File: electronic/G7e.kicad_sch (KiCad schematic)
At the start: 17 parts

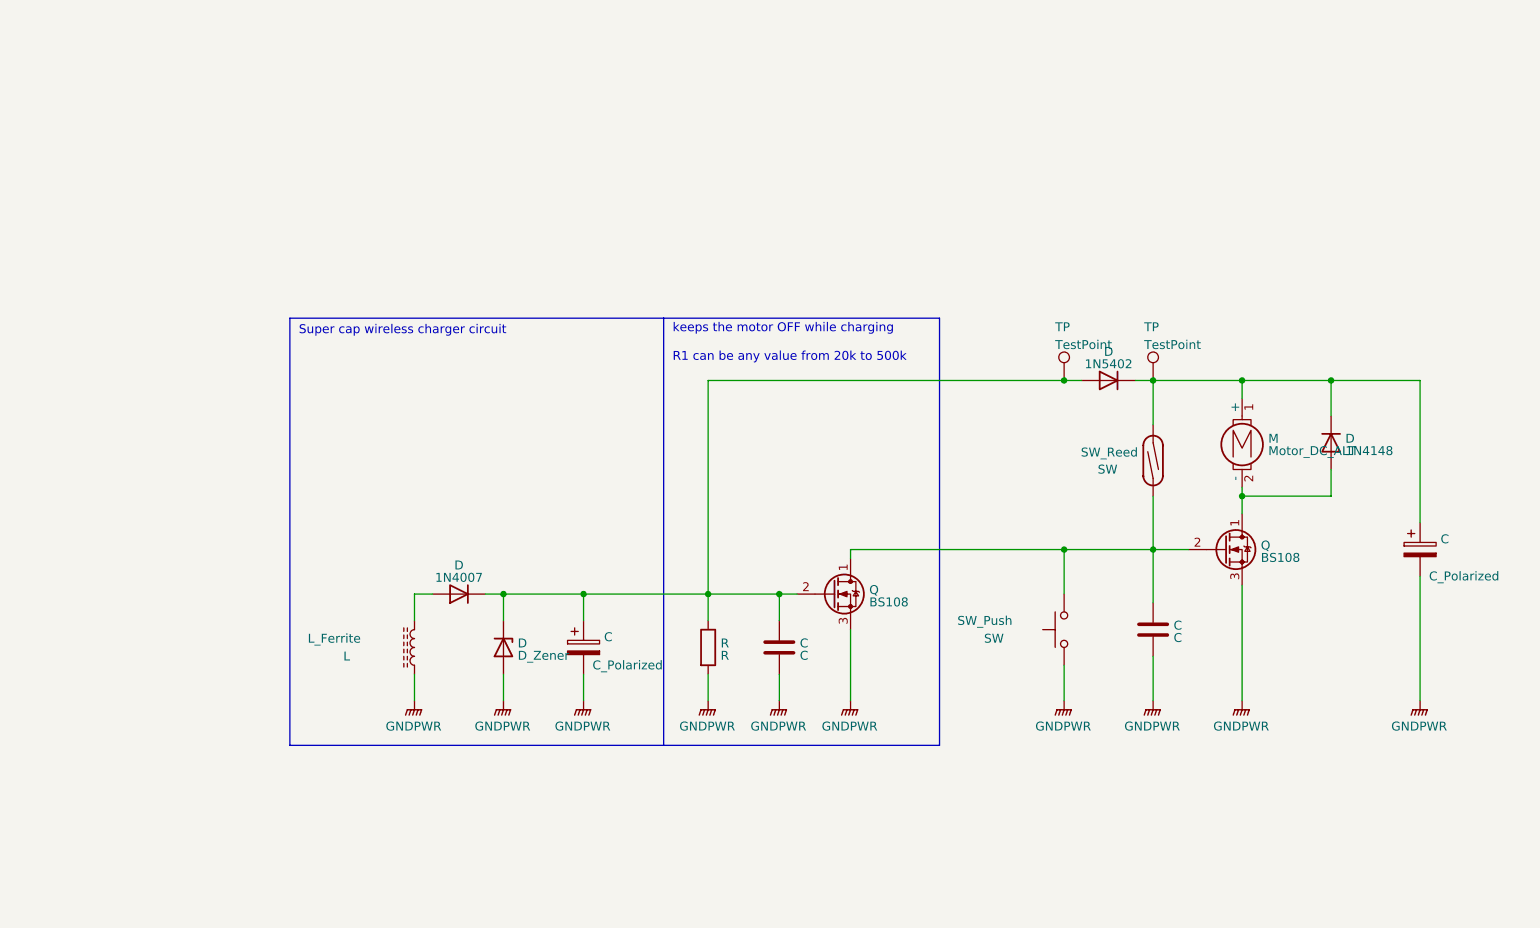
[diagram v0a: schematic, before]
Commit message: Adding propellers mockup
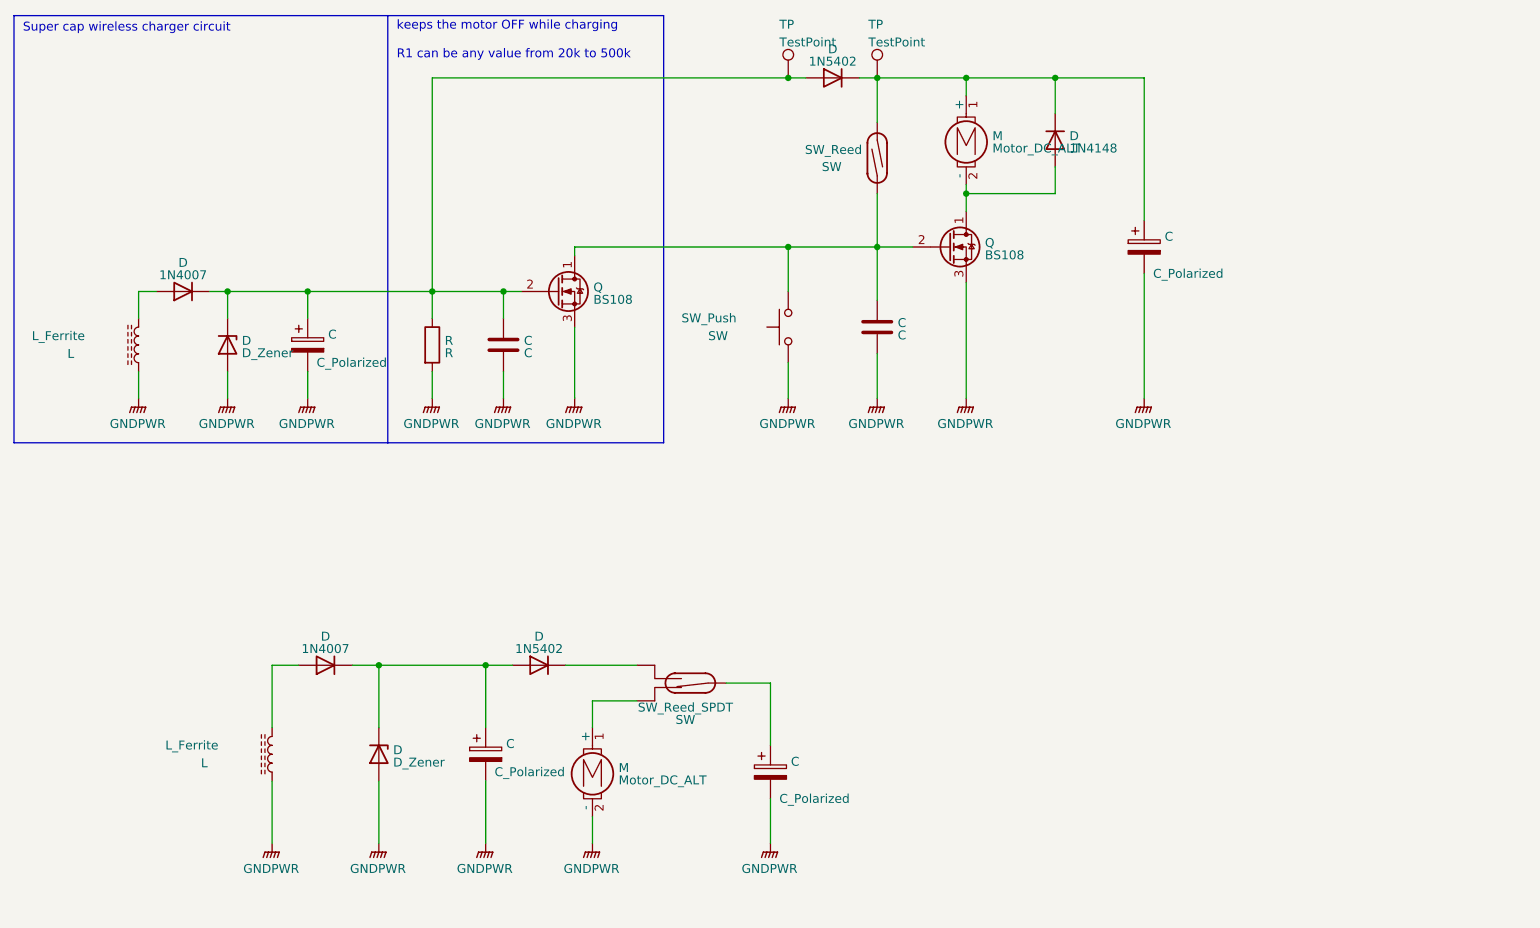
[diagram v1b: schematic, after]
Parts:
- added C (x2): C_Polarized, symbol Device:C_Polarized
- added D: 1N5402, Diode_THT:D_DO-201AD_P15.24mm_Horizontal, symbol Diode:1N5402
- added D: D_Zener, symbol Device:D_Zener
- added D: 1N4007, Diode_THT:D_DO-41_SOD81_P10.16mm_Horizontal, symbol Diode:1N4007
- added L: L_Ferrite, symbol Device:L_Ferrite
- added M: Motor_DC_ALT, symbol Motor:Motor_DC_ALT
- added SW: SW_Reed_SPDT, symbol Switch:SW_Reed_SPDT
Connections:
- net GNDPWR: now also C.2, C.2, D.2 (A), L.2, M.2 (-)
- new net: C.1, SW.2
- new net: D.1 (K), SW.3
- new net: C.1, D.1 (K), D.1 (K), D.2 (A)
- new net: M.1 (+), SW.1
- new net: D.2 (A), L.1
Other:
- moved on the sheet: C, D, L, M, Q, R, SW, TP

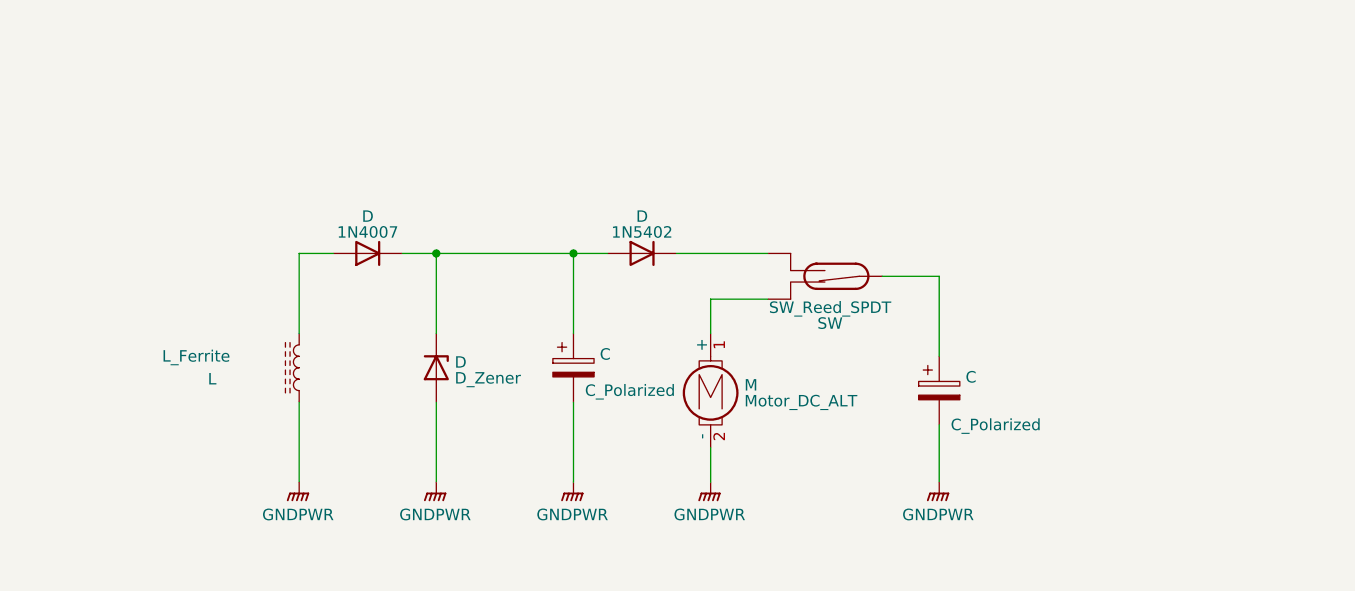
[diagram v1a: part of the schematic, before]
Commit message: Adding simplified electrical circuit
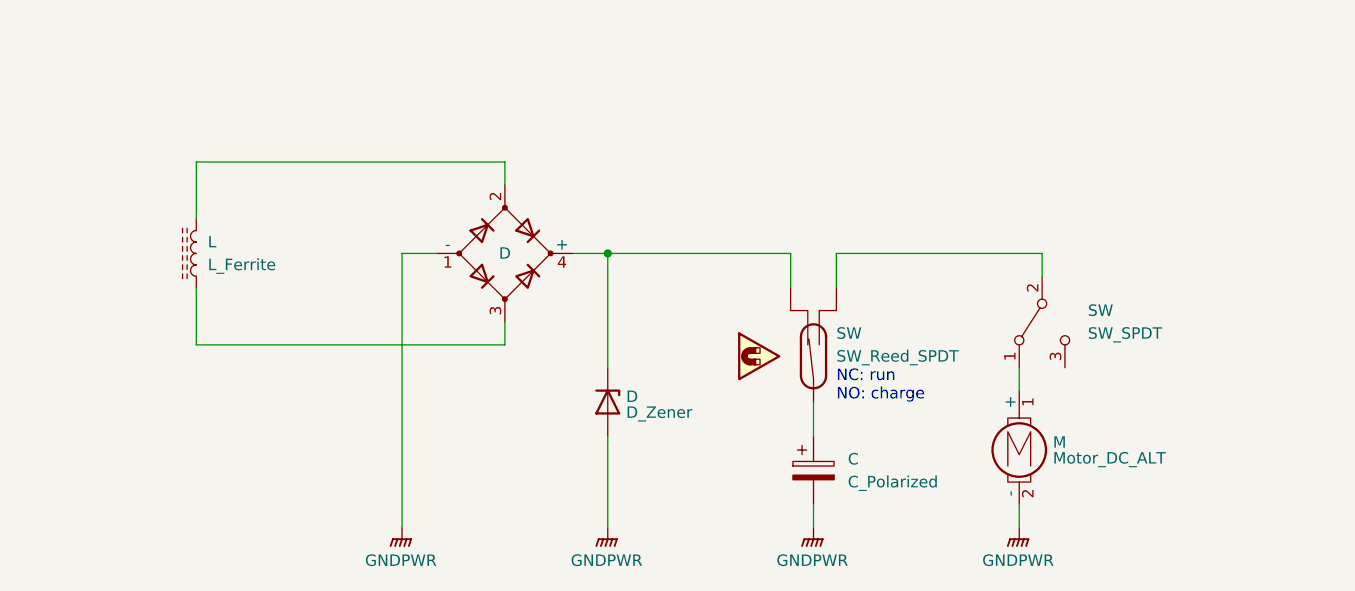
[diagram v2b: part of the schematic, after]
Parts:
- removed C: C_Polarized, symbol Device:C_Polarized
- removed D: 1N5402, Diode_THT:D_DO-201AD_P15.24mm_Horizontal, symbol Diode:1N5402
- removed D: 1N4007, Diode_THT:D_DO-41_SOD81_P10.16mm_Horizontal, symbol Diode:1N4007
- added D: D_Bridge_-AA+, symbol Device:D_Bridge_-AA+
- added SW: SW_SPDT, symbol Switch:SW_SPDT
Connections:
- net GNDPWR: now also D.1 (-); no longer L.2
- net at SW.3: now also SW.2 (B)
- net at D.1 (K): now also SW.1, D.4 (+)
- net at M.1 (+): now also SW.1 (A); no longer SW.1
- net at L.1: now also D.2
- new net: D.3, L.2
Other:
- note added: "NC: run NO: charge"
- moved on the sheet: C, D, L, M, SW

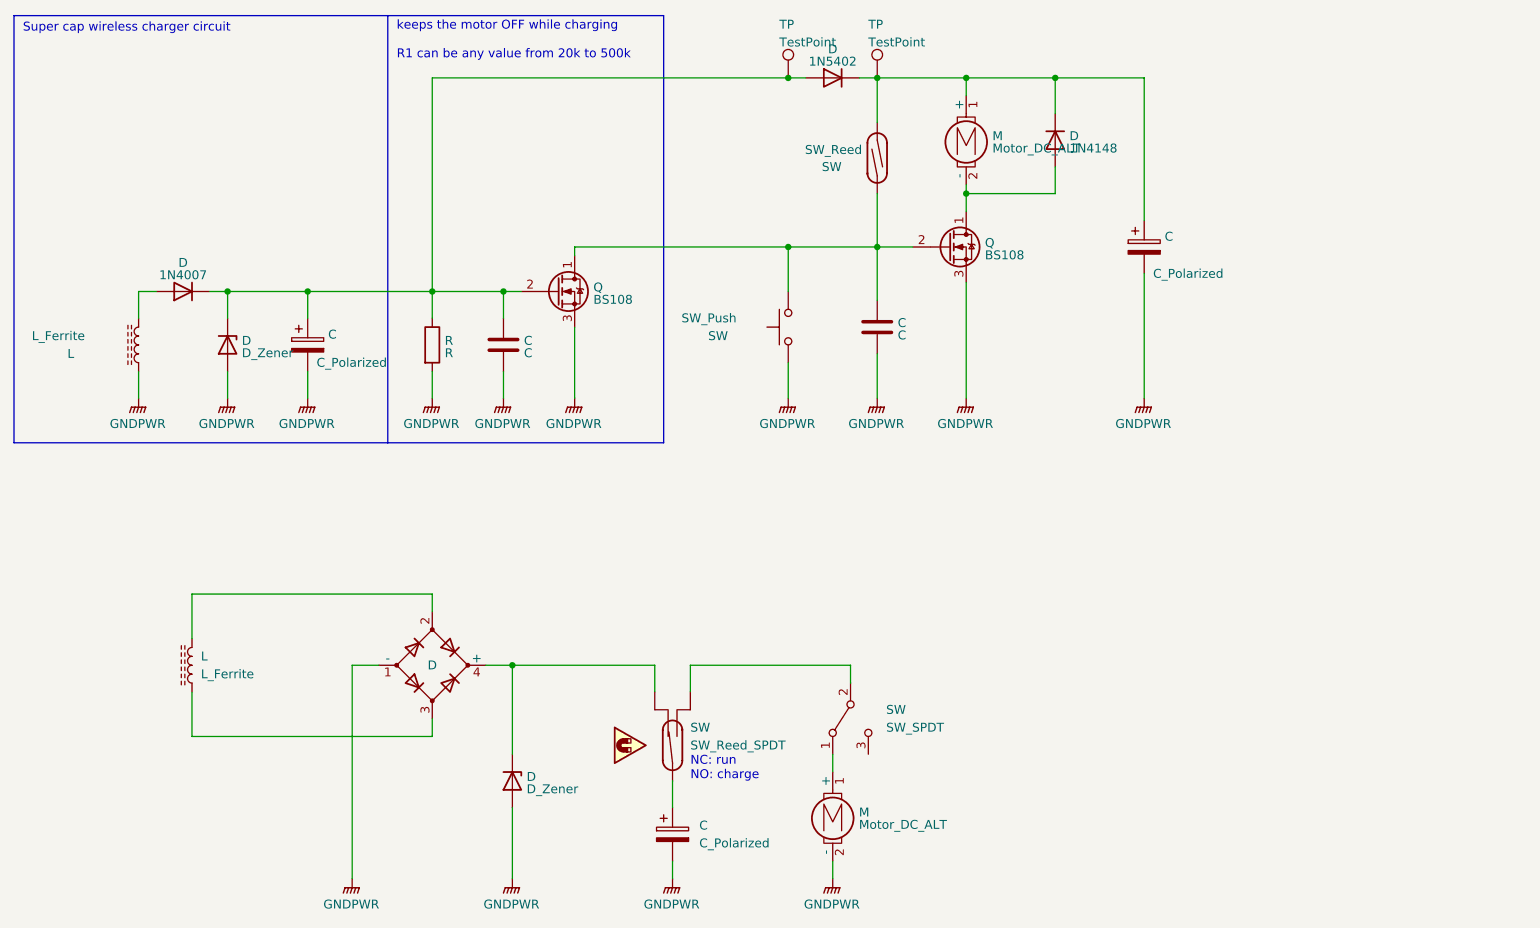
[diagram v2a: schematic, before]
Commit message: Separating schematics in each own sheet
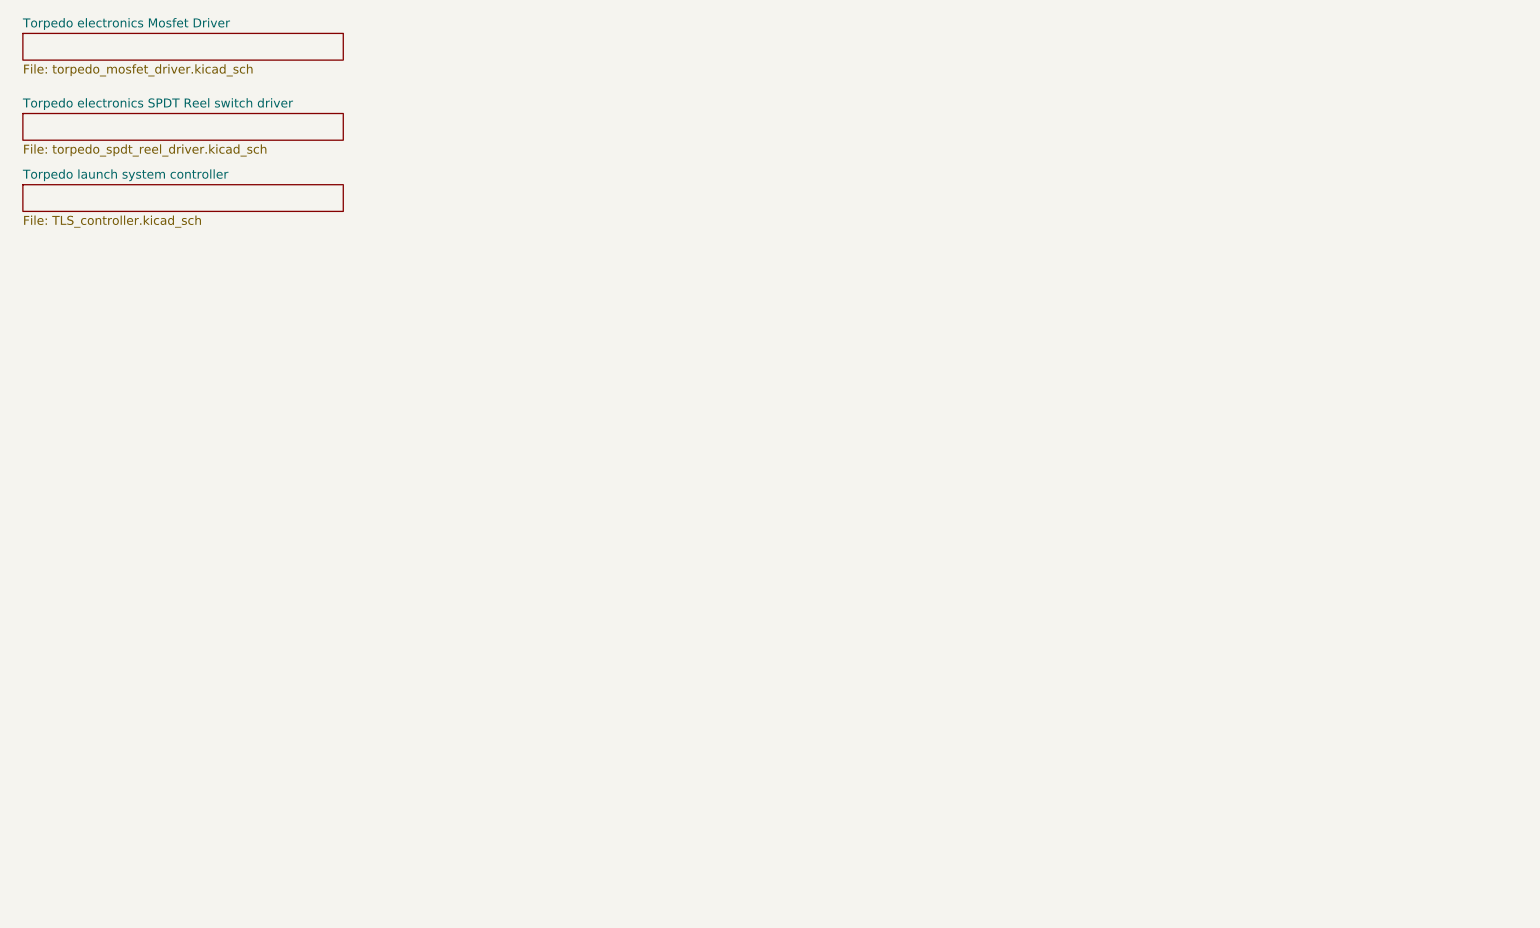
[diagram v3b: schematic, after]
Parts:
- removed C (x3): C_Polarized, symbol Device:C_Polarized
- removed C (x2): C, symbol Device:C
- removed D: D_Bridge_-AA+, symbol Device:D_Bridge_-AA+
- removed D: 1N4148, Diode_THT:D_DO-35_SOD27_P7.62mm_Horizontal, symbol Diode:1N4148
- removed D (x2): D_Zener, symbol Device:D_Zener
- removed D: 1N4007, Diode_THT:D_DO-41_SOD81_P10.16mm_Horizontal, symbol Diode:1N4007
- removed D: 1N5402, Diode_THT:D_DO-201AD_P15.24mm_Horizontal, symbol Diode:1N5402
- removed L (x2): L_Ferrite, symbol Device:L_Ferrite
- removed M (x2): Motor_DC_ALT, symbol Motor:Motor_DC_ALT
- removed Q (x2): BS108, Package_TO_SOT_THT:TO-92_Inline, symbol Transistor_FET:BS108
- removed R: R, symbol Device:R
- removed SW: SW_Push, symbol Switch:SW_Push
- removed SW: SW_Reed_SPDT, symbol Switch:SW_Reed_SPDT
- removed SW: SW_SPDT, symbol Switch:SW_SPDT
- removed SW: SW_Reed, symbol Switch:SW_Reed
- removed TP (x2): TestPoint, symbol Connector:TestPoint
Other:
- added sheet Torpedo electronics Mosfet Driver (torpedo_mosfet_driver.kicad_sch)
- added sheet Torpedo electronics SPDT Reel switch driver (torpedo_spdt_reel_driver.kicad_sch)
- added sheet Torpedo launch system controller (TLS_controller.kicad_sch)
- note removed: "NC: run NO: charge"
- note removed: "Super cap wireless charger circuit"
- note removed: "keeps the motor OFF while charging R1 can be any value from 20k to 500k"
